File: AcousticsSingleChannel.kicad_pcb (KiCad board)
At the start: 4 copper layers, 25.4 x 44.1 mm, 59 parts, among them J1 87233-3, J2 87233-3, J3 87233-3, J8 22-05-3021, SW2 Switch_Omron_A6S-1104-PH_eec, U1 OPA1604AIPWR, U2 OPA1604AIPWR, U3 LTC6910-3CTS8#TRPBF, U4 LTC1197LIMS8#PBF

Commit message: Ready for review
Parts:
- removed ? (x6): , AltiumImports:Probepoint
- removed G*** (x3): LOGO, LOGO
- removed J3: 87233-3, AltiumImports:TE_87233-3
- removed J8: 22-05-3021, AltiumImports:FP-22-05-3021-MFG
- removed SW2: Switch_Omron_A6S-1104-PH_eec, AltiumImports:Omron_A6S-1104-PH_0
- added C19: 1.5nF, AltiumImports:SMD-0603C, B.Cu at (147.5, 108.3)
- added R18: 25, AltiumImports:SMD-0603-RES, B.Cu at (145.8, 110.3)
- C11, C12, C13, C14, C15, C16, C17: moved to B.Cu
- C18: value 2.2µF -> 1µF; moved to B.Cu
- J1: value 87233-3 -> SSW-104-01-G-D; footprint AltiumImports:TE_87233-3 -> Accoustics:SAMTEC_SSW-104-01-G-D; moved to B.Cu
- J2: value 87233-3 -> TSW-104-07-F-D; footprint AltiumImports:TE_87233-3 -> Accoustics:SAMTEC_TSW-104-07-F-D; moved to B.Cu
- R26: value 750 -> 0; moved to B.Cu
- R27: value 1k -> 0; moved to B.Cu
- U4: value LTC1197LIMS8#PBF -> ADS7042IDCUR; footprint AltiumImports:FP-MS8-8-05-08-1660-IPC_A -> Accoustics:DCU0008A_L; moved to B.Cu
- moved J1 29.9 mm to (144.6, 83.1), turned to 180 degrees
- moved R1 19.9 mm to (146.3, 99.4), turned to -90 degrees
- moved C15 19.3 mm to (149.4, 86.8)
- moved R3 19.2 mm to (149.4, 99.4), turned to -90 degrees
- moved C13 16.1 mm to (152.8, 106.6)
- moved R8 15.3 mm to (145.3, 96.1), turned to 180 degrees
- moved R5 15.0 mm to (152.6, 85.5), turned to -90 degrees
- moved R2 15.0 mm to (153.2, 95.8), turned to 0 degrees
- moved R10 14.7 mm to (143.7, 96.1), turned to 180 degrees
- moved R26 13.4 mm to (150.0, 115.0), turned to 0 degrees
- moved C3 12.6 mm to (143.7, 91.7), turned to 180 degrees
- moved C5 12.6 mm to (145.5, 91.7), turned to 180 degrees
- moved U4 12.2 mm to (150.2, 110.4), turned to 90 degrees
- moved C18 12.0 mm to (150.2, 105.8), turned to 90 degrees
- moved R25 11.4 mm to (148.2, 85.9), turned to 180 degrees
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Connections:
- net Net-(U1A-IN_A+) renamed /BufferBiasAmp/BUF_IN
- C12 pad 2: VCC -> +3.3V
- C13 pad 1: VCC -> +3.3V
- C14 pad 2: VCC -> +3.3V
- C15 pad 2: VCC -> +3.3V
- C16 pad 2: VCC -> +3.3V
- C17 pad 2: VCC -> +3.3V
- C18 pad 1: VCC -> +3.3V
- C2 pad 1: /BufferBiasAmp/BBA_IN -> /Hydro+
- R21 pad 2: Net-(R21-Pad2) -> /Mode_Sel
- R25 pad 2: VCC -> +3.3V
- R26 pad 1: Net-(J2-Pad1) -> Net-(J2-Pad05)
- R26 pad 2: Net-(U4-ADC_DOUT) -> Net-(U4-SDO)
- R27 pad 2: Net-(J2-Pad1) -> Net-(J2-Pad05)
- R5 pad 1: /BufferBiasAmp/BBA_IN -> /Hydro+
- R5 pad 2: Net-(R21-Pad2) -> /Mode_Sel
- U1 pad 4: VCC -> +3.3V
- U2 pad 4: VCC -> +3.3V
- U3 pad 5: /OutputAmplifier/G0_out -> /G0_out
- U3 pad 6: /OutputAmplifier/G1_out -> /G1_out
- U3 pad 7: /OutputAmplifier/G2_out -> /G2_out
- U3 pad 8: VCC -> +3.3V
- U4 pad 1: Net-(U4-~{CS}) -> +3.3V
- U4 pad 2: /Sig_Out -> Net-(U4-SCLK)
- U4 pad 3: GND -> Net-(U4-SDO)
- U4 pad 4: GND -> Net-(U4-CS_N)
- U4 pad 5: VCC -> GND
- U4 pad 6: Net-(U4-ADC_DOUT) -> Net-(U4-AINP)
- U4 pad 7: Net-(U4-CLK) -> +3.3V
- U4 pad 8: VCC -> GND
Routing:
- net +3.3V: track 0.00 -> 83.8 mm, vias 0 -> 3
- net /Mode_Sel: track 0.00 -> 45.3 mm, vias 0 -> 2
- net /G2_out: track 0.00 -> 36.7 mm, vias 0 -> 1
- net /G1_out: track 0.00 -> 36.1 mm, vias 0 -> 1
- net /G0_out: track 0.00 -> 35.7 mm, vias 0 -> 1
- net VCC: track 29.7 -> 0.00 mm, vias 7 -> 0
- net GND: track 36.4 -> 9.25 mm, vias 9 -> 8
- net Net-(U4-~{CS}): track 23.4 -> 0.00 mm
- net Net-(U4-CLK): track 20.0 -> 0.00 mm
- net /BufferBiasAmp/BBA_IN: track 19.3 -> 0.00 mm
- net Net-(J2-Pad1): track 19.3 -> 0.00 mm
- net /OutputAmplifier/G2_out: track 17.4 -> 0.00 mm
- net /OutputAmplifier/G1_out: track 15.1 -> 0.00 mm
- net /OutputAmplifier/G0_out: track 12.8 -> 0.00 mm
- net /Band Pass Filter/F3_Out: track 19.1 -> 6.60 mm
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- added copper zone on B.Cu, net GND
- removed copper zone on B.Cu, net VCC
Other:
- board size 25.4 x 44.1 mm -> 11.7 x 44.1 mm
- board text removed: "AMP"
- board text removed: "Acoustics Single Channel PCB"
- board text removed: "BBA"
- board text removed: "F1"
- board text removed: "F2"
- board text removed: "F3"
- board text removed: "F4"
- board text removed: "GND"
- board text removed: "HYDROPHONE"
- board text removed: "v1.1.2"

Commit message: Ready for Review.
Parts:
- removed C10, C8, C9: 1000pF, AltiumImports:SMD-0603C
- removed C17: 1µF, AltiumImports:SMD-0603C
- removed C19: 1.5nF, AltiumImports:SMD-0603C
- removed R10: 698, AltiumImports:SMD-0603-RES
- removed R11: 536, AltiumImports:SMD-0603-RES
- removed R12: 165k, AltiumImports:SMD-0603-RES
- removed R13: 86.6k, AltiumImports:SMD-0603-RES
- removed R14: 11k, AltiumImports:SMD-0603-RES
- removed R15: 5.76k, AltiumImports:SMD-0603-RES
- removed R16: 332, AltiumImports:SMD-0603-RES
- removed R17: 174, AltiumImports:SMD-0603-RES
- removed R18: 25, AltiumImports:SMD-0603-RES
- removed R7: 41.2k, AltiumImports:SMD-0603-RES
- removed R8: 17.4k, AltiumImports:SMD-0603-RES
- removed R9: 13k, AltiumImports:SMD-0603-RES
- removed U4: ADS7042IDCUR, Accoustics:DCU0008A_L
- added TP1: 5005, Accoustics:KEYSTONE_5005, F.Cu at (144.9, 99.7)
- added TP3: 5005, Accoustics:KEYSTONE_5005, F.Cu at (151.7, 107.4)
- added TP4: 5006, Accoustics:KEYSTONE_5006, F.Cu at (144.9, 104.7)
- C13: value 1µF -> .1µF
- C3, C4, C6: value 1000pF -> 1µF; moved to B.Cu
- C5: value 1000pF -> 0F
- C7: value 1000pF -> .1µF; moved to B.Cu
- R26, R27: moved to F.Cu
- R6: value 54.9k -> 0
- U2: value OPA1604AIPWR -> ADS127L21IRUKT; footprint AltiumImports:PW0014A_N -> Accoustics:WQFN20_RUK_TEX
- moved C3 21.1 mm to (144.7, 112.8), turned to 90 degrees
- moved R6 19.2 mm to (148.8, 107.5), turned to 0 degrees
- moved C5 16.3 mm to (145.6, 108.0), turned to 90 degrees
- moved C6 14.5 mm to (147.2, 116.1), turned to -90 degrees
- moved C11 13.6 mm to (150.4, 98.1)
- moved C4 13.4 mm to (144.7, 114.1)
- moved C12 13.2 mm to (150.9, 102.2), turned to 90 degrees
- moved U3 12.8 mm to (150.8, 101.8)
- moved C7 11.6 mm to (151.8, 116.3), turned to 90 degrees
- moved R3 10.9 mm to (143.5, 90.2), turned to 0 degrees
- moved C18 7.90 mm to (144.7, 111.6)
- moved R1 6.72 mm to (143.5, 93.3), turned to 0 degrees
- moved C13 6.23 mm to (153.2, 112.8), turned to 180 degrees
- moved U2 5.45 mm to (148.1, 112.6), turned to -90 degrees
- moved R27 4.40 mm to (151.3, 116.8), turned to -90 degrees
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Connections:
- C12 pad 2: +3.3V -> +5V
- C13 pad 1: +3.3V -> +5V
- C14 pad 2: +3.3V -> +5V
- C15 pad 2: +3.3V -> +5V
- C16 pad 2: +3.3V -> +5V
- C18 pad 1: +3.3V -> +5V
- C3 pad 1: /Band Pass Filter/F1_In -> Net-(U2-CAPA)
- C3 pad 2: /Band Pass Filter/F1_Out -> GND
- C4 pad 1: /Band Pass Filter/F2_In -> Net-(U2-CAPD)
- C4 pad 2: /Band Pass Filter/F2_Out -> GND
- C5 pad 1: /Band Pass Filter/F1_In -> GND
- C5 pad 2: Net-(U1B-IN_B-) -> Net-(U2-AINP)
- C6 pad 1: /Band Pass Filter/F2_In -> GND
- C6 pad 2: Net-(U2A-IN_A-) -> +3.3V
- C7 pad 1: /Band Pass Filter/F3_In -> GND
- C7 pad 2: /Band Pass Filter/F3_Out -> +3.3V
- J2 pad 01: unconnected-(J2-Pad01) -> /CS
- J2 pad 02: unconnected-(J2-Pad02) -> /RESET
- J2 pad 03: Net-(U4-CS_N) -> /SCLK
- J2 pad 04: unconnected-(J2-Pad04) -> /SDI
- J2 pad 05: Net-(J2-Pad05) -> /CLK
- J2 pad 06: unconnected-(J2-Pad06) -> Net-(J2-Pad06)
- J2 pad 07: Net-(U4-SCLK) -> /START
- R2 pad 1: Net-(U1D-IN_D-) -> Net-(U1B-IN_B-)
- R25 pad 2: +3.3V -> +5V
- R26 pad 1: Net-(J2-Pad05) -> Net-(J2-Pad06)
- R26 pad 2: Net-(U4-SDO) -> /DOUT
- R27 pad 2: Net-(J2-Pad05) -> Net-(J2-Pad06)
- R4 pad 2: Net-(U1D-IN_D-) -> Net-(U1B-IN_B-)
- R6 pad 1: Net-(U1B-IN_B-) -> /Sig_Out
- R6 pad 2: /Band Pass Filter/F1_Out -> Net-(U2-AINP)
- U1 pad 12: AGND -> /OutputAmplifier/Amp_Out
- U1 pad 13: Net-(U1D-IN_D-) -> /Sig_Out
- U1 pad 14: /BufferBiasAmp/BBAmp_IN -> /Sig_Out
- U1 pad 4: +3.3V -> +5V
- U1 pad 7: /Band Pass Filter/F1_Out -> /BufferBiasAmp/BBAmp_IN
- U2 pad 1: /Band Pass Filter/F2_Out -> Net-(U2-AINP)
- U2 pad 10: AGND -> /DOUT
- U2 pad 11: GND -> unconnected-(U2-*DRDY-Pad11)
- U2 pad 12: AGND -> /CLK
- U2 pad 13: Net-(U2D-IN_D-) -> +3.3V
- U2 pad 14: /Band Pass Filter/F3_Out -> GND
- U2 pad 2: Net-(U2A-IN_A-) -> GND
- U2 pad 3: AGND -> unconnected-(U2-VCM-Pad3)
- U2 pad 4: +3.3V -> +5V
- U2 pad 5: /OutputAmplifier/Amp_Out -> GND
- U2 pad 6: /Sig_Out -> /RESET
- U2 pad 7: /Sig_Out -> /CS
- U2 pad 8: /Band Pass Filter/BPF_OUT -> /SDI
- U2 pad 9: Net-(U2C-IN_C-) -> /SCLK
- U3 pad 3: /Band Pass Filter/BPF_OUT -> /BufferBiasAmp/BBA_OUT
- U3 pad 8: +3.3V -> +5V
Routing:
- net +5V: track 0.00 -> 73.5 mm, vias 0 -> 4
- net +3.3V: track 83.8 -> 46.2 mm, vias 3 -> 1
- net AGND: track 25.3 -> 9.55 mm, vias 9 -> 10
- net /Band Pass Filter/F1_Out: track 15.5 -> 0.00 mm
- net GND: track 9.25 -> 23.5 mm, vias 8 -> 6
- net /Sig_Out: track 3.08 -> 16.8 mm, vias 1 -> 0
- net /Band Pass Filter/BPF_OUT: track 13.5 -> 0.00 mm
- net /BufferBiasAmp/BBA_OUT: track 4.47 -> 17.7 mm
- net /G2_out: track 36.7 -> 24.0 mm
- net /RESET: track 0.00 -> 11.9 mm
- net /G1_out: track 36.1 -> 24.7 mm
- net /SDI: track 0.00 -> 10.3 mm
- net /G0_out: track 35.7 -> 25.5 mm
- net Net-(J2-Pad06): track 0.00 -> 9.96 mm
- net /START: track 0.00 -> 9.76 mm
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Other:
- board text added: "BBA"
- board text added: "SIG"

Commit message: Ready for Review.
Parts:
- added R7: 0, AltiumImports:SMD-0603-RES, B.Cu at (150.5, 95.4)
- added R8: 0, AltiumImports:SMD-0603-RES, B.Cu at (150.5, 92.8)
- added U4: mcp1416t-e/ot, Accoustics:SOT-23-5_MC_MCH-M, B.Cu at (145.5, 95.1)
- moved C14 0.38 mm to (152.3, 86.3)
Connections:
- R21 pad 2: /Mode_Sel -> /Mode_Sel_Out
- R5 pad 2: /Mode_Sel -> /Mode_Sel_Out
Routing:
- net +3.3V: track 46.2 -> 65.0 mm, vias 1 -> 2
- net /Mode_Sel_Out: track 0.00 -> 18.0 mm, vias 0 -> 2
- net /Mode_Sel: track 43.7 -> 29.6 mm, vias 2 -> 1
- net Net-(U4-VDD): track 0.00 -> 12.9 mm
- net +5V: track 73.5 -> 79.5 mm

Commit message: Ready for Review.
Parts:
- moved J2 0.32 mm to (148.4, 120.1)
- moved J1 0.15 mm to (144.6, 83.0)
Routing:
- net /START: track 9.76 -> 7.91 mm
- net /RESET: track 11.9 -> 12.7 mm

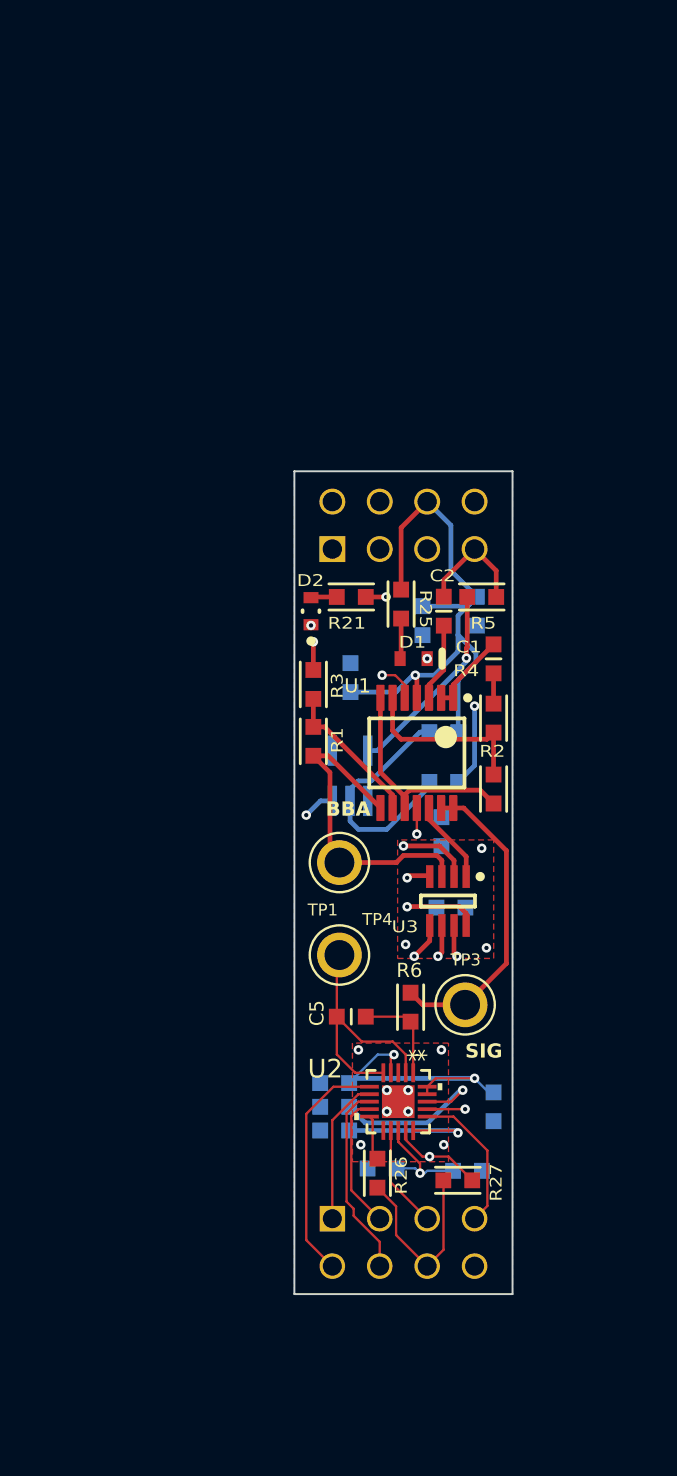
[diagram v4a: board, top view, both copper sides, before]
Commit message: Changed headers.
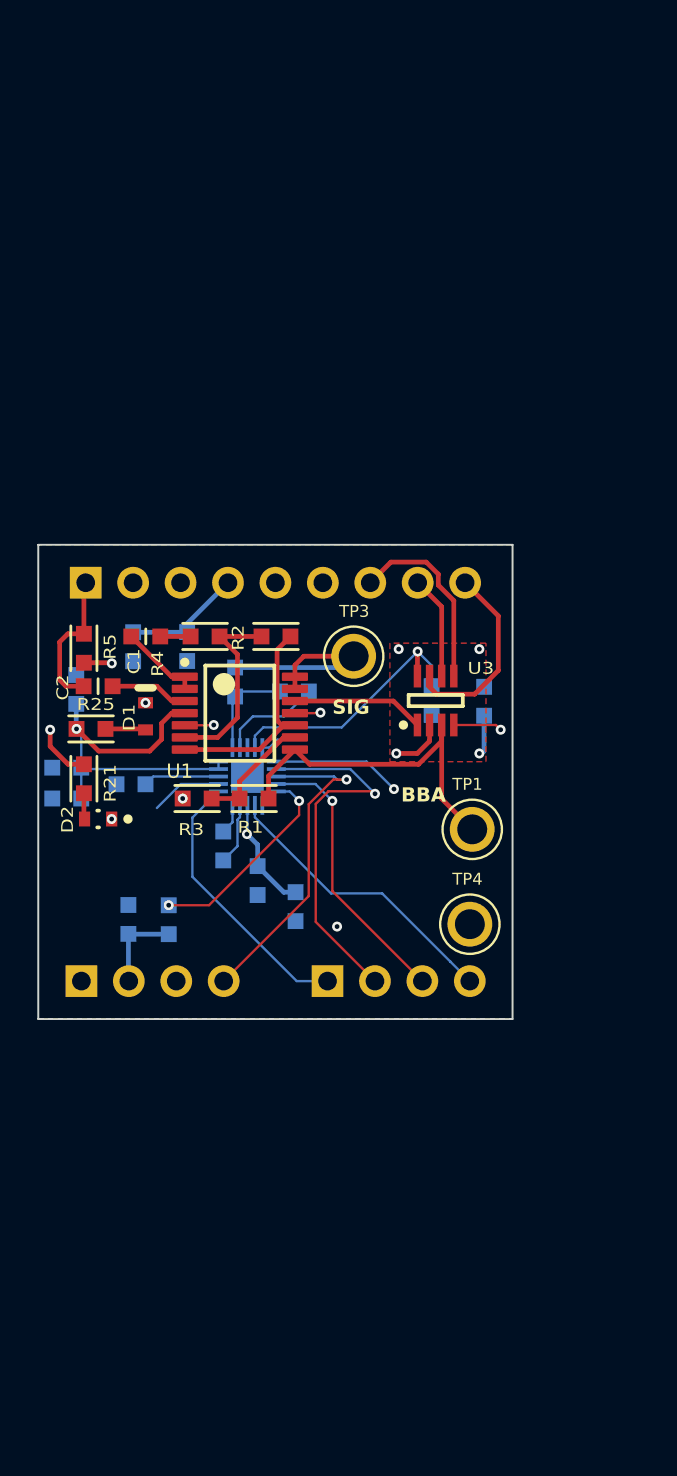
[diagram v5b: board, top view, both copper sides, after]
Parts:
- removed R7, R8: 0, AltiumImports:SMD-0603-RES
- removed U4: mcp1416t-e/ot, Accoustics:SOT-23-5_MC_MCH-M
- added J4: Conn_01x09_Pin, Connector_PinHeader_2.54mm:PinHeader_1x09_P2.54mm_Vertical, B.Cu at (131.4, 84.8)
- C5, R26, R27, R6, U2: moved to B.Cu
- J1: value SSW-104-01-G-D -> Conn_01x04_Pin; footprint Accoustics:SAMTEC_SSW-104-01-G-D -> Connector_PinHeader_2.54mm:PinHeader_1x04_P2.54mm_Vertical
- J2: value TSW-104-07-F-D -> Conn_01x04_Pin; footprint Accoustics:SAMTEC_TSW-104-07-F-D -> Connector_PinHeader_2.54mm:PinHeader_1x04_P2.54mm_Vertical
- moved C13 28.2 mm to (130.3, 96.3), turned to 90 degrees
- moved J1 26.8 mm to (131.1, 106.1), turned to -90 degrees
- moved R27 22.5 mm to (133.6, 102.8), turned to 180 degrees
- moved C18 22.2 mm to (130.3, 94.7)
- moved R5 21.5 mm to (131.3, 88.3), turned to 0 degrees
- moved C3 20.4 mm to (133.8, 95.6)
- moved R6 19.8 mm to (139.4, 90.1), turned to 180 degrees
- moved TP3 19.6 mm to (145.7, 88.7)
- moved U2 19.2 mm to (140.0, 95.1)
- moved C2 18.9 mm to (132.0, 90.3), turned to 90 degrees
- moved C1 18.7 mm to (134.6, 87.6), turned to -90 degrees
- moved C14 18.5 mm to (133.9, 88.2)
- moved R25 17.9 mm to (131.6, 92.6), turned to -90 degrees
- moved C5 17.7 mm to (142.5, 90.6)
- moved R26 17.6 mm to (135.8, 102.8), turned to 0 degrees
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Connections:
- net /Mode_Sel_Out renamed /Mode_Sel_5
- R26 pad 1: Net-(J2-Pad06) -> Net-(J1-Pin_2)
- R27 pad 2: Net-(J2-Pad06) -> Net-(J1-Pin_2)
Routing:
- net +3.3V: track 64.7 -> 21.0 mm, vias 2 -> 1
- net +5V: track 79.8 -> 41.7 mm, vias 4 -> 2
- net /Mode_Sel: track 29.9 -> 0.00 mm, vias 1 -> 0
- net /G1_out: track 24.8 -> 5.53 mm, vias 1 -> 0
- net /G0_out: track 25.7 -> 10.2 mm, vias 1 -> 0
- net /G2_out: track 24.2 -> 10.4 mm, vias 1 -> 0
- net Net-(U4-VDD): track 12.9 -> 0.00 mm
- net /CS: track 7.84 -> 20.1 mm, vias 0 -> 1
- net Net-(J2-Pad06): track 10.3 -> 0.00 mm
- net /CLK: track 5.53 -> 15.8 mm
- net /RESET: track 12.7 -> 22.9 mm, vias 0 -> 1
- net /DOUT: track 2.43 -> 11.2 mm, vias 0 -> 2
- net GND: track 23.5 -> 32.2 mm, vias 6 -> 5
- net /SCLK: track 7.29 -> 15.0 mm, vias 0 -> 1
- net /SDI: track 10.4 -> 17.8 mm, vias 0 -> 1
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- added copper zone on In1.Cu, net +5V
- removed copper zone on In1.Cu, net GND
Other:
- board size 11.7 x 44.1 mm -> 25.4 x 25.4 mm

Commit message: spacing
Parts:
- moved TP4 0.13 mm to (151.9, 102.9)
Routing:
- net /CS: track 20.1 -> 15.9 mm
- net /G0_out: track 10.2 -> 11.2 mm
- net /RESET: track 22.9 -> 23.8 mm
- net /START: track 14.7 -> 15.2 mm
